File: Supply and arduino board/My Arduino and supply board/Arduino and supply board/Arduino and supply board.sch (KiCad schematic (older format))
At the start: 70 parts, among them J1 USB_C_Receptacle_USB2.0, J2 Conn_01x03, J3 Conn_01x03, J4 Conn_01x03, J5 Conn_01x03, J6 Conn_01x03, J7 Conn_01x03, J8 Programing_port, J9 Conn_01x05, Q2 16MHz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

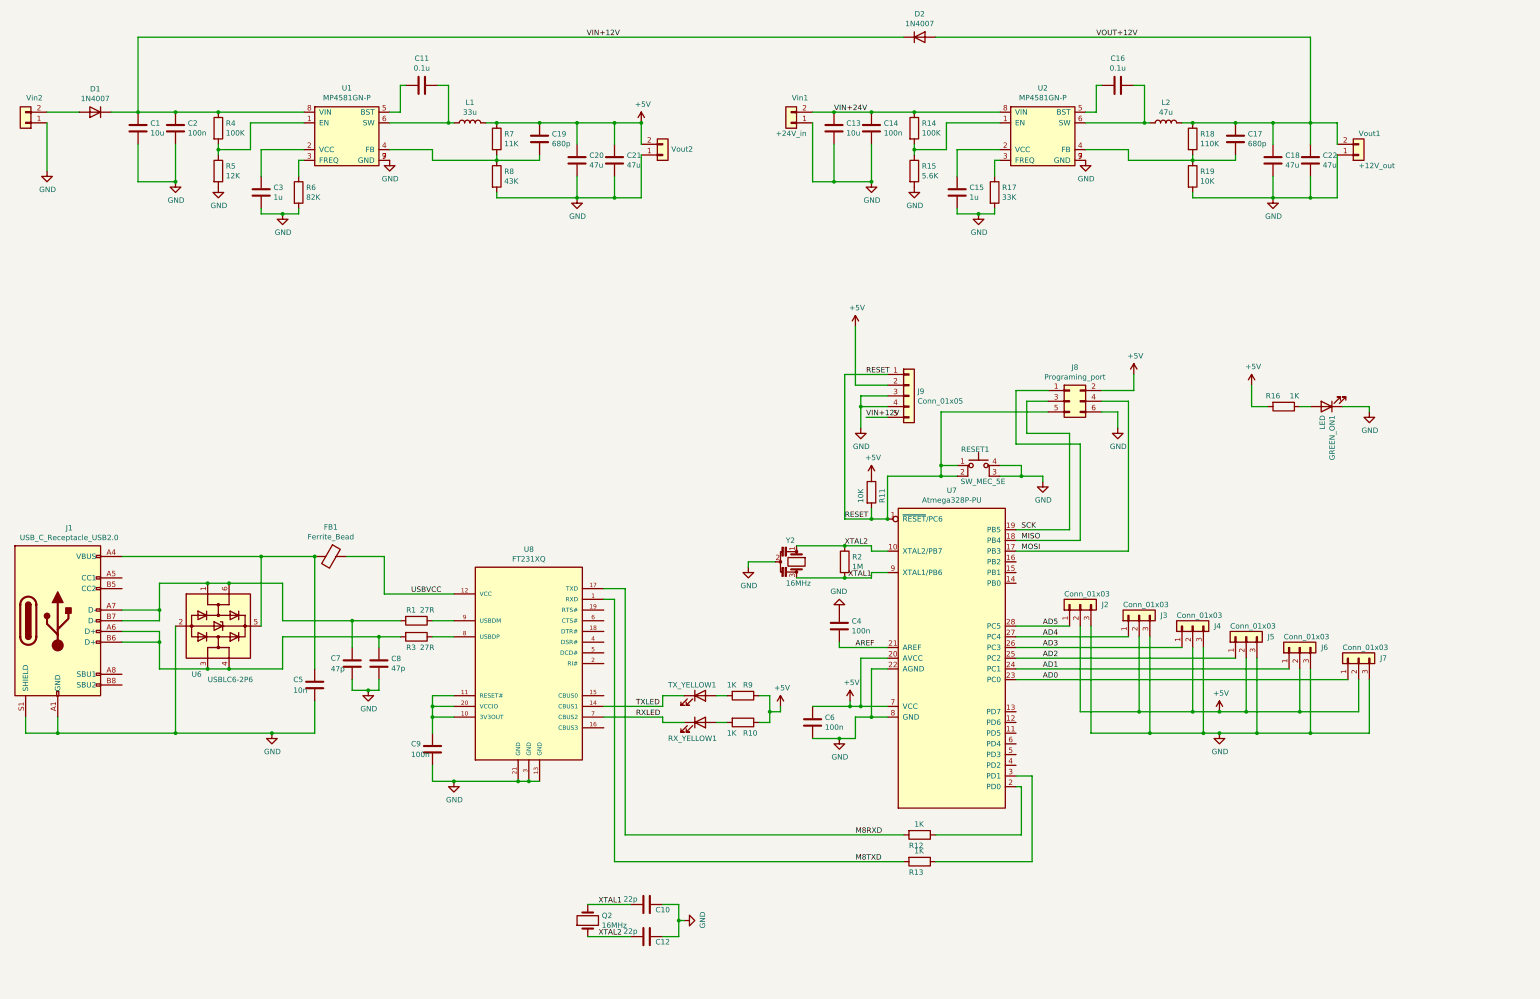
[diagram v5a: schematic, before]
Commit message: generate blueprints for lose part feeder
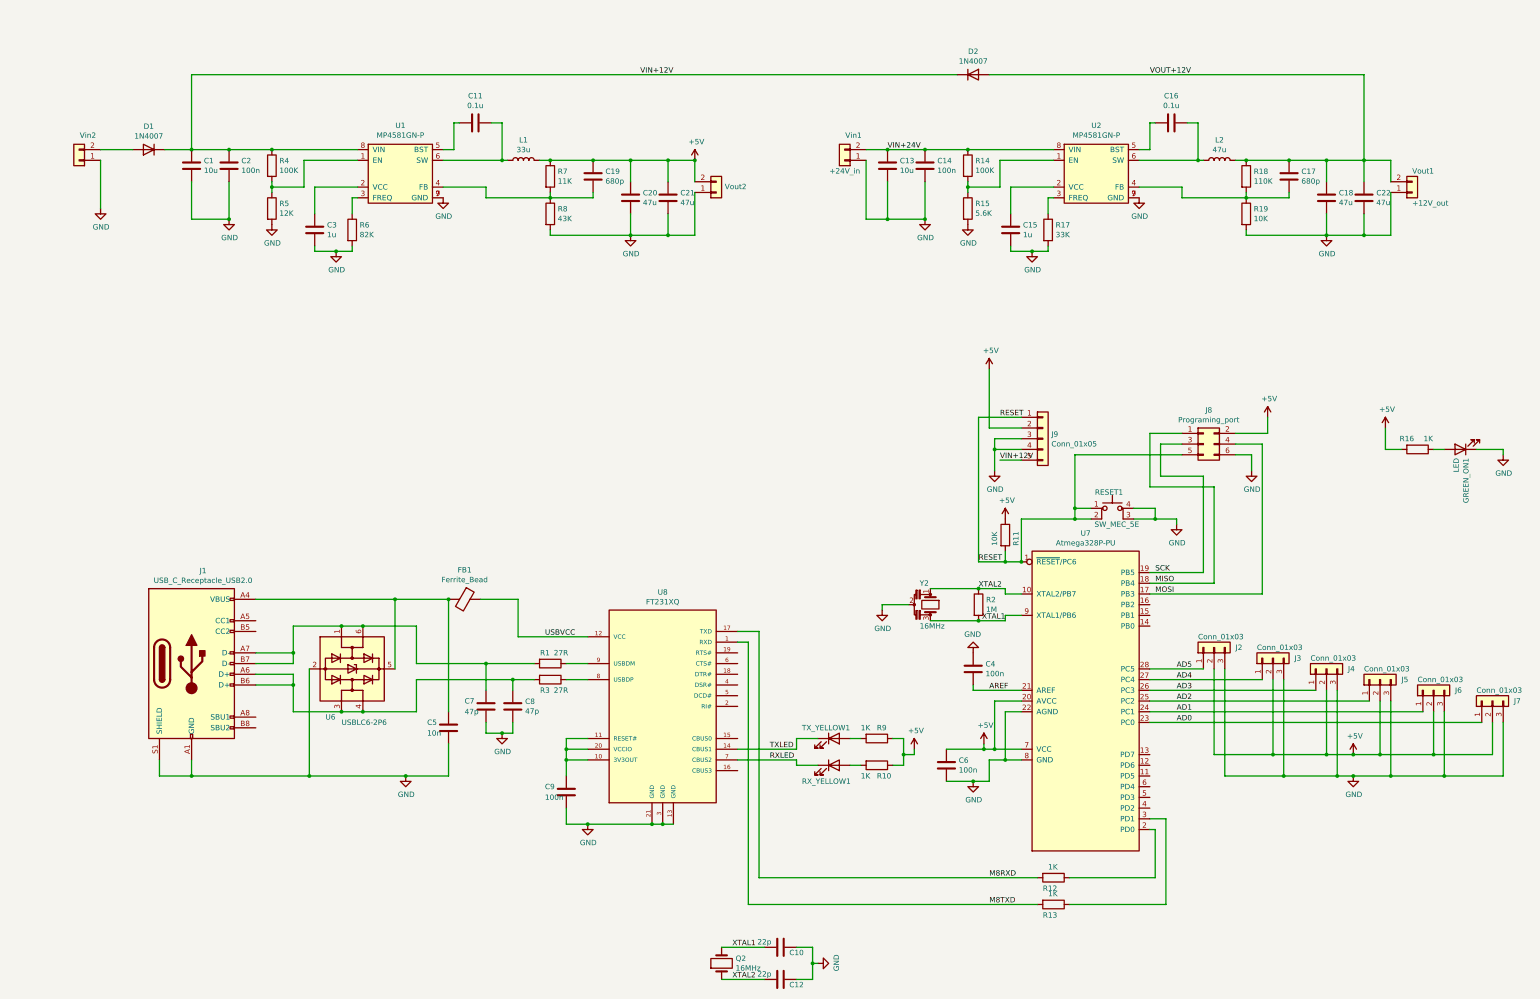
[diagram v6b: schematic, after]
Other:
- moved on the sheet: C1, C10, C11, C12, C13, C14, C15, C16, C17, C18, C19, C2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

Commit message: changes on powersuply
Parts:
- removed R15: 5.6K, Resistor_SMD:R_0402_1005Metric, symbol Device:R
- removed R5: 12K, Resistor_SMD:R_0402_1005Metric, symbol Device:R
- removed U1, U2: MP4581GN-P, Package_SO:SOIC-8-1EP_3.9x4.9mm_P1.27mm_EP2.514x3.2mm, symbol Assembly_board_schem:MP4581GN-P
- added U1, U2: TD2786MR, Package_SO:SOP-8_3.9x4.9mm_P1.27mm, symbol Assembly_board_schem:TD2786MR
- C15, C3: value 1u -> 0.1u
- C16: value 0.1u -> 10n
- C17: value 680p -> 3.9u
- C19: value 680p -> 3.9n
- L1: value 33u -> 220uH/1.6A; footprint Inductor_SMD:L_Wuerth_HCI-1040 -> Inductor_SMD:L_Wuerth_HCI-1350
- L2: value 47u -> 220uH/1.6A; footprint Inductor_SMD:L_Wuerth_HCM-1350 -> Inductor_SMD:L_Wuerth_HCI-1350
- R17: value 33K -> 6.8K
- R19: value 10K -> 9K
- R6: value 82K -> 6.8K
- R8: value 43K -> 2.4K
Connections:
- net +5V: no longer C19.2
- net GND: now also C17.2, C19.2, U1.4 (GND), U1.9 (GND), U2.4 (GND), U2.9 (GND); no longer R17.2, R6.2
- net VIN+12V: now also U1.2 (VIN)
- net VIN+24V: now also U2.2 (VIN)
- net VOUT+12V: no longer C17.2
- net at C15.1: now also U2.8 (SS)
- net at C16.1, L2.1: now also U2.3 (LX)
- net at C16.2: now also U2.1 (BS)
- net at R18.2, R19.1: now also U2.5 (FB); no longer C17.1
- net at R14.2: now also U2.7 (EN)
- net at R17.1: now also U2.6 (COMP)
- net at C3.1: now also U1.8 (SS)
- net at C11.1, L1.1: now also U1.3 (LX)
- net at C11.2: now also U1.1 (BS)
- net at R7.2, R8.1: now also U1.5 (FB); no longer C19.1
- net at R4.2: now also U1.7 (EN)
- net at R6.1: now also U1.6 (COMP)
- new net: C19.1, R17.2
- new net: C17.1, R6.2
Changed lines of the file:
@@
 P 10050 2700
 F 0 "C15" H 10165 2746 50  0000 L CNN
-F 1 "1u" H 10165 2655 50  0000 L CNN
+F 1 "0.1u" H 10165 2655 50  0000 L CNN
 F 2 "Capacitor_SMD:C_0603_1608Metric" H 10088 2550 50  0001 C CNN
 F 3 "~" H 10050 2700 50  0001 C CNN
@@
 P 11550 1700
 F 0 "C16" V 11298 1700 50  0000 C CNN
-F 1 "0.1u" V 11389 1700 50  0000 C CNN
+F 1 "10n" V 11389 1700 50  0000 C CNN
 F 2 "Capacitor_SMD:C_0603_1608Metric" H 11588 1550 50  0001 C CNN
 F 3 "~" H 11550 1700 50  0001 C CNN
 	1    11550 1700
 	0    1    1    0
-$EndComp
-$Comp
-L Device:C C17
-U 1 1 657293B3
-P 12650 2200
-F 0 "C17" H 12535 2154 50  0000 R CNN
-F 1 "680p" H 12535 2245 50  0000 R CNN
-F 2 "Capacitor_SMD:C_0603_1608Metric" H 12688 2050 50  0001 C CNN
-F 3 "~" H 12650 2200 50  0001 C CNN
-	1    12650 2200
-	-1   0    0    1
 $EndComp
 $Comp
@@
 P 12000 2050
 F 0 "L2" V 12190 2050 50  0000 C CNN
-F 1 "47u" V 12099 2050 50  0000 C CNN
-F 2 "Inductor_SMD:L_Wuerth_HCM-1350" H 12000 2050 50  0001 C CNN
+F 1 "220uH/1.6A" V 12099 2050 50  0000 C CNN
+F 2 "Inductor_SMD:L_Wuerth_HCI-1350" H 12000 2050 50  0001 C CNN
 F 3 "~" H 12000 2050 50  0001 C CNN
 	1    12000 2050
@@
 P 12250 2550
 F 0 "R19" H 12320 2596 50  0000 L CNN
-F 1 "10K" H 12320 2505 50  0000 L CNN
+F 1 "9K" H 12320 2505 50  0000 L CNN
 F 2 "Resistor_SMD:R_0402_1005Metric" V 12180 2550 50  0001 C CNN
 F 3 "~" H 12250 2550 50  0001 C CNN
@@
 Wire Wire Line
 	12150 2050 12250 2050
-Wire Wire Line
-	12250 2050 12650 2050
 Connection ~ 12250 2050
-Wire Wire Line
-	12650 2050 13000 2050
-Connection ~ 12650 2050
 Wire Wire Line
 	13000 2250 13000 2050
@@
 Connection ~ 13000 2750
 Wire Wire Line
-	12650 2400 12250 2400
-Wire Wire Line
 	11650 2400 11650 2300
 Wire Wire Line
 	11650 2300 11250 2300
-Wire Wire Line
-	12650 2400 12650 2350
 Wire Wire Line
 	12250 2350 12250 2400
@@
 	13350 1250 9850 1250
 $Comp
-L Assembly_board_schem:MP4581GN-P U2
-U 1 1 658409AE
-P 10850 2150
-F 0 "U2" H 10850 2575 50  0000 C CNN
-F 1 "MP4581GN-P" H 10850 2484 50  0000 C CNN
-F 2 "Package_SO:SOIC-8-1EP_3.9x4.9mm_P1.27mm_EP2.514x3.2mm" H 10850 2150 50  0001 C CNN
-F 3 "" H 10850 2150 50  0001 C CNN
-	1    10850 2150
-	1    0    0    -1
-$EndComp
-$Comp
 L Device:R R14
 U 1 1 6582C206
@@
 	1    0    0    -1
 $EndComp
-$Comp
-L Device:R R15
-U 1 1 6582CDAE
-P 9650 2500
-F 0 "R15" H 9720 2546 50  0000 L CNN
-F 1 "5.6K" H 9720 2455 50  0000 L CNN
-F 2 "Resistor_SMD:R_0402_1005Metric" V 9580 2500 50  0001 C CNN
-F 3 "~" H 9650 2500 50  0001 C CNN
-	1    9650 2500
-	1    0    0    -1
-$EndComp
 Wire Wire Line
 	9950 2300 9650 2300
 Wire Wire Line
 	9650 2300 9650 2250
-Wire Wire Line
-	9650 2350 9650 2300
-Connection ~ 9650 2300
 Wire Wire Line
 	12250 2700 12250 2750
@@
 Wire Wire Line
 	9950 2050 10450 2050
-$Comp
-L power:GND #PWR0117
-U 1 1 658C02C0
-P 9650 2650
-F 0 "#PWR0117" H 9650 2400 50  0001 C CNN
-F 1 "GND" H 9655 2477 50  0000 C CNN
-F 2 "" H 9650 2650 50  0001 C CNN
-F 3 "" H 9650 2650 50  0001 C CNN
-	1    9650 2650
-	1    0    0    -1
-$EndComp
 $Comp
 L Device:R R17
@@
 P 10400 2700
 F 0 "R17" H 10470 2746 50  0000 L CNN
-F 1 "33K" H 10470 2655 50  0000 L CNN
+F 1 "6.8K" H 10470 2655 50  0000 L CNN
 F 2 "Resistor_SMD:R_0402_1005Metric" V 10330 2700 50  0001 C CNN
 F 3 "~" H 10400 2700 50  0001 C CNN
@@
 	10050 2300 10050 2550
 Wire Wire Line
-	10050 2850 10050 2900
-Wire Wire Line
-	10050 2900 10250 2900
-Wire Wire Line
 	10400 2900 10400 2850
-$Comp
-L power:GND #PWR0118
-U 1 1 658FFE1C
-P 10250 2900
-F 0 "#PWR0118" H 10250 2650 50  0001 C CNN
-F 1 "GND" H 10255 2727 50  0000 C CNN
-F 2 "" H 10250 2900 50  0001 C CNN
-F 3 "" H 10250 2900 50  0001 C CNN
-	1    10250 2900
-	1    0    0    -1
-$EndComp
-Connection ~ 10250 2900
-Wire Wire Line
-	10250 2900 10400 2900
 $Comp
 L Device:C C22
@@
 P 3550 2700
 F 0 "C3" H 3665 2746 50  0000 L CNN
-F 1 "1u" H 3665 2655 50  0000 L CNN
+F 1 "0.1u" H 3665 2655 50  0000 L CNN
 F 2 "Capacitor_SMD:C_0603_1608Metric" H 3588 2550 50  0001 C CNN
 F 3 "~" H 3550 2700 50  0001 C CNN
@@
 $EndComp
 $Comp
-L Device:C C19
-U 1 1 6590ACF2
-P 6150 2200
-F 0 "C19" H 6035 2154 50  0000 R CNN
-F 1 "680p" H 6035 2245 50  0000 R CNN
-F 2 "Capacitor_SMD:C_0603_1608Metric" H 6188 2050 50  0001 C CNN
-F 3 "~" H 6150 2200 50  0001 C CNN
-	1    6150 2200
-	-1   0    0    1
-$EndComp
-$Comp
 L Connector_Generic:Conn_01x02 Vout2
 U 1 1 6590ACF8
@@
 P 5500 2050
 F 0 "L1" V 5690 2050 50  0000 C CNN
-F 1 "33u" V 5599 2050 50  0000 C CNN
-F 2 "Inductor_SMD:L_Wuerth_HCI-1040" H 5500 2050 50  0001 C CNN
+F 1 "220uH/1.6A" V 5599 2050 50  0000 C CNN
+F 2 "Inductor_SMD:L_Wuerth_HCI-1350" H 5500 2050 50  0001 C CNN
 F 3 "~" H 5500 2050 50  0001 C CNN
 	1    5500 2050
@@
 P 5750 2550
 F 0 "R8" H 5820 2596 50  0000 L CNN
-F 1 "43K" H 5820 2505 50  0000 L CNN
+F 1 "2.4K" H 5820 2505 50  0000 L CNN
 F 2 "Resistor_SMD:R_0402_1005Metric" V 5680 2550 50  0001 C CNN
 F 3 "~" H 5750 2550 50  0001 C CNN
@@
 Wire Wire Line
 	5650 2050 5750 2050
-Wire Wire Line
-	5750 2050 6150 2050
 Connection ~ 5750 2050
-Wire Wire Line
-	6150 2050 6500 2050
-Connection ~ 6150 2050
 Wire Wire Line
 	6500 2250 6500 2050
@@
 Connection ~ 6500 2750
 Wire Wire Line
-	6150 2400 5750 2400
-Wire Wire Line
 	5150 2400 5150 2300
 Wire Wire Line
 	5150 2300 4750 2300
-Wire Wire Line
-	6150 2400 6150 2350
 Wire Wire Line
 	5750 2350 5750 2400
@@
 $EndComp
 $Comp
-L Assembly_board_schem:MP4581GN-P U1
-U 1 1 6590AD4E
-P 4350 2150
-F 0 "U1" H 4350 2575 50  0000 C CNN
-F 1 "MP4581GN-P" H 4350 2484 50  0000 C CNN
-F 2 "Package_SO:SOIC-8-1EP_3.9x4.9mm_P1.27mm_EP2.514x3.2mm" H 4350 2150 50  0001 C CNN
-F 3 "" H 4350 2150 50  0001 C CNN
-	1    4350 2150
-	1    0    0    -1
-$EndComp
-$Comp
 L Device:R R4
 U 1 1 6590AD54
@@
 	1    0    0    -1
 $EndComp
-$Comp
-L Device:R R5
-U 1 1 6590AD5A
-P 3150 2500
-F 0 "R5" H 3220 2546 50  0000 L CNN
-F 1 "12K" H 3220 2455 50  0000 L CNN
-F 2 "Resistor_SMD:R_0402_1005Metric" V 3080 2500 50  0001 C CNN
-F 3 "~" H 3150 2500 50  0001 C CNN
-	1    3150 2500
-	1    0    0    -1
-$EndComp
 Wire Wire Line
 	3450 2300 3150 2300
 Wire Wire Line
 	3150 2300 3150 2250
-Wire Wire Line
-	3150 2350 3150 2300
-Connection ~ 3150 2300
 Wire Wire Line
 	5750 2700 5750 2750
@@
 Wire Wire Line
 	3450 2050 3950 2050
-$Comp
-L power:GND #PWR0123
-U 1 1 6590AD6B
-P 3150 2650
-F 0 "#PWR0123" H 3150 2400 50  0001 C CNN
-F 1 "GND" H 3155 2477 50  0000 C CNN
-F 2 "" H 3150 2650 50  0001 C CNN
-F 3 "" H 3150 2650 50  0001 C CNN
-	1    3150 2650
-	1    0    0    -1
-$EndComp
 $Comp
 L Device:R R6
@@
 P 3900 2700
 F 0 "R6" H 3970 2746 50  0000 L CNN
-F 1 "82K" H 3970 2655 50  0000 L CNN
+F 1 "6.8K" H 3970 2655 50  0000 L CNN
 F 2 "Resistor_SMD:R_0402_1005Metric" V 3830 2700 50  0001 C CNN
 F 3 "~" H 3900 2700 50  0001 C CNN
@@
 	3550 2300 3550 2550
 Wire Wire Line
-	3550 2850 3550 2900
-Wire Wire Line
-	3550 2900 3750 2900
-Wire Wire Line
 	3900 2900 3900 2850
-$Comp
-L power:GND #PWR0124
-U 1 1 6590AD7E
-P 3750 2900
-F 0 "#PWR0124" H 3750 2650 50  0001 C CNN
-F 1 "GND" H 3755 2727 50  0000 C CNN
-F 2 "" H 3750 2900 50  0001 C CNN
-F 3 "" H 3750 2900 50  0001 C CNN
-	1    3750 2900
-	1    0    0    -1
-$EndComp
-Connection ~ 3750 2900
-Wire Wire Line
-	3750 2900 3900 2900
 $Comp
 L Device:C C21
@@
 Wire Wire Line
 	9750 4450 9750 5800
+$Comp
+L Assembly_board_schem:TD2786MR U1
+U 1 1 6590E12E
+P 4350 2150
+F 0 "U1" H 4350 2575 50  0000 C CNN
+F 1 "TD2786MR" H 4350 2484 50  0000 C CNN
+F 2 "Package_SO:SOP-8_3.9x4.9mm_P1.27mm" H 4350 2150 50  0001 C CNN
+F 3 "" H 4350 2150 50  0001 C CNN
+	1    4350 2150
+	1    0    0    -1
+$EndComp
+$Comp
+L Assembly_board_schem:TD2786MR U2
+U 1 1 6590EA1B
+P 10850 2150
+F 0 "U2" H 10850 2575 50  0000 C CNN
+F 1 "TD2786MR" H 10850 2484 50  0000 C CNN
+F 2 "Package_SO:SOP-8_3.9x4.9mm_P1.27mm" H 10850 2150 50  0001 C CNN
+F 3 "" H 10850 2150 50  0001 C CNN
+	1    10850 2150
+	1    0    0    -1
+$EndComp
+$Comp
+L Device:C C19
+U 1 1 65929436
+P 10400 3050
+F 0 "C19" H 10515 3096 50  0000 L CNN
+F 1 "3.9n" H 10515 3005 50  0000 L CNN
+F 2 "Capacitor_SMD:C_0603_1608Metric" H 10438 2900 50  0001 C CNN
+F 3 "~" H 10400 3050 50  0001 C CNN
+	1    10400 3050
+	1    0    0    -1
+$EndComp
+Wire Wire Line
+	12250 2050 13000 2050
+Wire Wire Line
+	10050 3250 10250 3250
+Wire Wire Line
+	10400 3250 10400 3200
+Wire Wire Line
+	10050 2850 10050 3250
+$Comp
+L power:GND #PWR0117
+U 1 1 65943132
+P 10250 3250
+F 0 "#PWR0117" H 10250 3000 50  0001 C CNN
+F 1 "GND" H 10255 3077 50  0000 C CNN
+F 2 "" H 10250 3250 50  0001 C CNN
+F 3 "" H 10250 3250 50  0001 C CNN
+	1    10250 3250
+	1    0    0    -1
+$EndComp
+Connection ~ 10250 3250
+Wire Wire Line
+	10250 3250 10400 3250
+Wire Wire Line
+	5750 2050 6500 2050
+$Comp
+L Device:C C17
+U 1 1 659438A7
+P 3900 3050
+F 0 "C17" H 4015 3096 50  0000 L CNN
+F 1 "3.9u" H 4015 3005 50  0000 L CNN
+F 2 "Capacitor_SMD:C_0603_1608Metric" H 3938 2900 50  0001 C CNN
+F 3 "~" H 3900 3050 50  0001 C CNN
+	1    3900 3050
+	1    0    0    -1
+$EndComp
+Wire Wire Line
+	3550 3250 3700 3250
+Wire Wire Line
+	3900 3250 3900 3200
+Wire Wire Line
+	3550 2850 3550 3250
+$Comp
+L power:GND #PWR0118
+U 1 1 6595CD16
+P 3700 3250
+F 0 "#PWR0118" H 3700 3000 50  0001 C CNN
+F 1 "GND" H 3705 3077 50  0000 C CNN
+F 2 "" H 3700 3250 50  0001 C CNN
+F 3 "" H 3700 3250 50  0001 C CNN
+	1    3700 3250
+	1    0    0    -1
+$EndComp
+Connection ~ 3700 3250
+Wire Wire Line
+	3700 3250 3900 3250
 $EndSCHEMATC
